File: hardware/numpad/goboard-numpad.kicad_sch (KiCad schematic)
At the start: 6 parts, among them J1 Conn_02x05_Top_Bottom, J2 Conn_01x01, J3 Conn_01x05, SW1 SW_Push

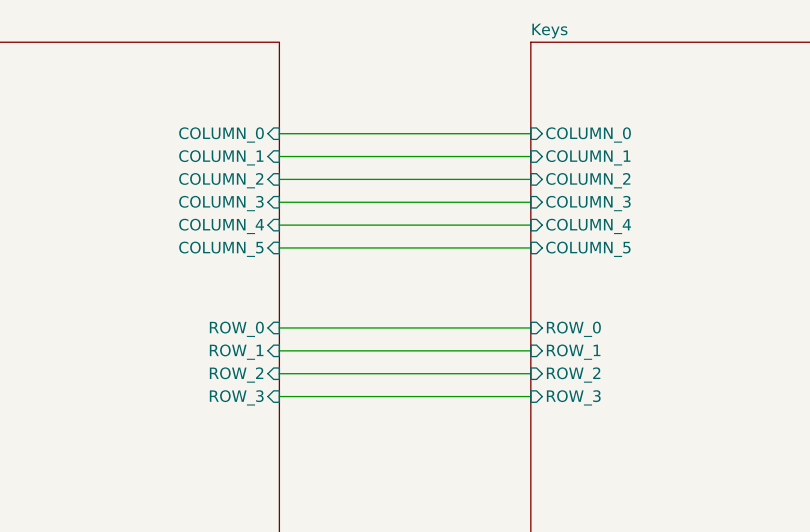
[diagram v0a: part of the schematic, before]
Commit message: Numpad: exchange key identifer
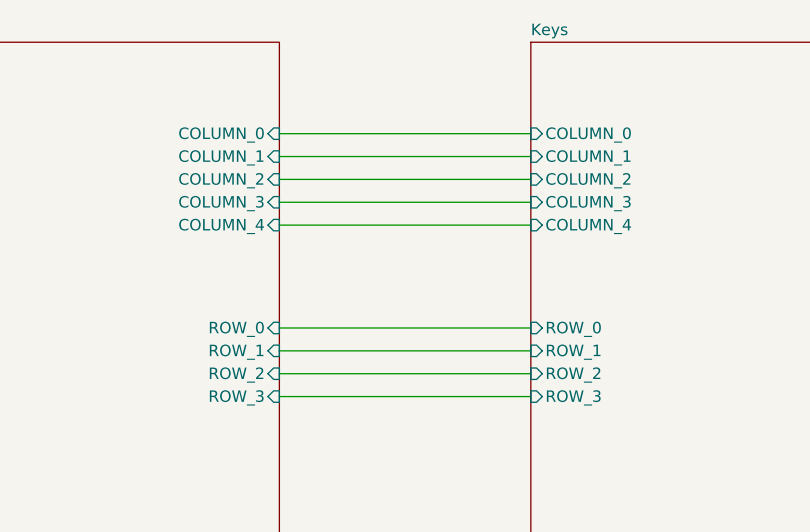
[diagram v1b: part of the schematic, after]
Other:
- sheet Keys ports: added none; removed COLUMN_5
- sheet mcu ports: added none; removed COLUMN_5
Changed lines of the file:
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@@
-    (stroke (width 0) (type solid) (color 0 0 0 0))
-  )
-  (wire (pts (xy 152.4 48.26) (xy 180.34 48.26))
     (stroke (width 0) (type solid) (color 0 0 0 0))
   )
@@
       (effects (font (size 1.27 1.27)) (justify left))
     )
-    (pin "COLUMN_5" input (at 180.34 48.26 180)
-      (effects (font (size 1.27 1.27)) (justify left))
-    )
     (pin "COLUMN_4" input (at 180.34 45.72 180)
       (effects (font (size 1.27 1.27)) (justify left))
@@
       (effects (font (size 1.27 1.27)) (justify left))
     )
-    (pin "COLUMN_5" input (at 152.4 48.26 0)
-      (effects (font (size 1.27 1.27)) (justify right))
-    )
     (pin "COLUMN_0" input (at 152.4 35.56 0)
       (effects (font (size 1.27 1.27)) (justify right))
@@
     )
     (path "/7cad715e-ebc0-41a5-9955-927ca63abd2f/6de5427d-4003-4de5-929c-849cf5d9ff9c"
-      (reference "SW8") (unit 1) (value "/") (footprint "footprints:SW_Cherry_MX_1.00u_PCB")
+      (reference "SW8") (unit 1) (value "divide") (footprint "footprints:SW_Cherry_MX_1.00u_PCB")
     )
     (path "/7cad715e-ebc0-41a5-9955-927ca63abd2f/72bf7a3c-a50c-4d69-90e7-2e5dba295699"
@@
     )
     (path "/7cad715e-ebc0-41a5-9955-927ca63abd2f/9b4a23f9-cd74-4ef8-8ec9-c324c0c6ccc0"
-      (reference "SW13") (unit 1) (value ".") (footprint "footprints:SW_Cherry_MX_1.00u_PCB")
+      (reference "SW13") (unit 1) (value "dot") (footprint "footprints:SW_Cherry_MX_1.00u_PCB")
     )
     (path "/7cad715e-ebc0-41a5-9955-927ca63abd2f/57a1dd78-2b07-42d9-8bd6-44368a92ec63"
-      (reference "SW14") (unit 1) (value "*") (footprint "footprints:SW_Cherry_MX_1.00u_PCB")
+      (reference "SW14") (unit 1) (value "times") (footprint "footprints:SW_Cherry_MX_1.00u_PCB")
     )
     (path "/7cad715e-ebc0-41a5-9955-927ca63abd2f/db6492b6-c0a9-4cb1-a618-b7fd084d31af"
@@
     )
     (path "/7cad715e-ebc0-41a5-9955-927ca63abd2f/4a471f23-a2bc-4fe0-b458-9d0b46d30813"
-      (reference "SW18") (unit 1) (value "-") (footprint "footprints:SW_Cherry_MX_1.00u_PCB")
+      (reference "SW18") (unit 1) (value "minus") (footprint "footprints:SW_Cherry_MX_1.00u_PCB")
     )
     (path "/7cad715e-ebc0-41a5-9955-927ca63abd2f/061c5f42-1869-4eb2-8fe0-4ae429f958da"
-      (reference "SW19") (unit 1) (value "+") (footprint "footprints:SW_Cherry_MX_2.00u_PCB")
+      (reference "SW19") (unit 1) (value "plus") (footprint "footprints:SW_Cherry_MX_2.00u_PCB")
     )
     (path "/7cad715e-ebc0-41a5-9955-927ca63abd2f/dcb7a6be-fb34-414c-ba21-e1f3767bdcea"

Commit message: Numpad: Fix labels of columns and rows of the key matrix
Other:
- sheet Keys ports: added ROW_4; removed COLUMN_4
- sheet mcu ports: added ROW_4; removed COLUMN_4
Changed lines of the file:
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@@
       (effects (font (size 1.27 1.27)) (justify left top))
     )
-    (pin "COLUMN_1" input (at 180.34 38.1 180)
+    (pin "COLUMN_1" input (at 180.34 59.69 180)
       (effects (font (size 1.27 1.27)) (justify left))
     )
-    (pin "COLUMN_0" input (at 180.34 35.56 180)
+    (pin "COLUMN_0" input (at 180.34 57.15 180)
       (effects (font (size 1.27 1.27)) (justify left))
     )
-    (pin "ROW_0" input (at 180.34 57.15 180)
+    (pin "ROW_0" input (at 180.34 35.56 180)
       (effects (font (size 1.27 1.27)) (justify left))
     )
-    (pin "ROW_1" input (at 180.34 59.69 180)
+    (pin "ROW_1" input (at 180.34 38.1 180)
       (effects (font (size 1.27 1.27)) (justify left))
     )
-    (pin "ROW_2" input (at 180.34 62.23 180)
+    (pin "ROW_2" input (at 180.34 40.64 180)
       (effects (font (size 1.27 1.27)) (justify left))
     )
-    (pin "ROW_3" input (at 180.34 64.77 180)
+    (pin "COLUMN_2" input (at 180.34 62.23 180)
       (effects (font (size 1.27 1.27)) (justify left))
     )
-    (pin "COLUMN_4" input (at 180.34 45.72 180)
+    (pin "COLUMN_3" input (at 180.34 64.77 180)
       (effects (font (size 1.27 1.27)) (justify left))
     )
-    (pin "COLUMN_2" input (at 180.34 40.64 180)
+    (pin "ROW_4" input (at 180.34 45.72 180)
       (effects (font (size 1.27 1.27)) (justify left))
     )
-    (pin "COLUMN_3" input (at 180.34 43.18 180)
+    (pin "ROW_3" input (at 180.34 43.18 180)
       (effects (font (size 1.27 1.27)) (justify left))
     )
@@
       (effects (font (size 1.27 1.27)) (justify left top))
     )
-    (pin "ROW_1" input (at 152.4 59.69 0)
+    (pin "ROW_1" input (at 152.4 38.1 0)
       (effects (font (size 1.27 1.27)) (justify right))
     )
-    (pin "ROW_2" input (at 152.4 62.23 0)
+    (pin "ROW_2" input (at 152.4 40.64 0)
       (effects (font (size 1.27 1.27)) (justify right))
     )
-    (pin "ROW_0" input (at 152.4 57.15 0)
+    (pin "ROW_0" input (at 152.4 35.56 0)
       (effects (font (size 1.27 1.27)) (justify right))
     )
-    (pin "ROW_3" input (at 152.4 64.77 0)
+    (pin "ROW_3" input (at 152.4 43.18 0)
       (effects (font (size 1.27 1.27)) (justify right))
     )
@@
       (effects (font (size 1.27 1.27)) (justify left))
     )
-    (pin "COLUMN_0" input (at 152.4 35.56 0)
+    (pin "COLUMN_0" input (at 152.4 57.15 0)
       (effects (font (size 1.27 1.27)) (justify right))
     )
-    (pin "COLUMN_4" input (at 152.4 45.72 0)
+    (pin "COLUMN_1" input (at 152.4 59.69 0)
       (effects (font (size 1.27 1.27)) (justify right))
     )
-    (pin "COLUMN_1" input (at 152.4 38.1 0)
+    (pin "COLUMN_3" input (at 152.4 64.77 0)
       (effects (font (size 1.27 1.27)) (justify right))
     )
-    (pin "COLUMN_3" input (at 152.4 43.18 0)
-      (effects (font (size 1.27 1.27)) (justify right))
-    )
-    (pin "COLUMN_2" input (at 152.4 40.64 0)
+    (pin "COLUMN_2" input (at 152.4 62.23 0)
       (effects (font (size 1.27 1.27)) (justify right))
     )
@@
       (effects (font (size 1.27 1.27)) (justify left))
     )
+    (pin "ROW_4" input (at 152.4 45.72 0)
+      (effects (font (size 1.27 1.27)) (justify right))
+    )
   )

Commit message: Numpad: Exchange the debug-conn footprint for one without silkscreen
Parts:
- J1: footprint footprints:programming_port_st_link_clone -> footprints:programming_port_st_link_clone_without_silkscreen_outline
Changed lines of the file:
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@@
     (property "Reference" "J1" (id 0) (at 52.07 111.76 0))
     (property "Value" "Conn_02x05_Top_Bottom" (id 1) (at 52.07 109.22 0))
-    (property "Footprint" "footprints:programming_port_st_link_clone" (id 2) (at 50.8 100.33 0)
+    (property "Footprint" "footprints:programming_port_st_link_clone_without_silkscreen_outline" (id 2) (at 50.8 100.33 0)
       (effects (font (size 1.27 1.27)) hide)
     )
@@
     )
     (path "/15258cf0-82ec-42ff-b81f-96479422bf94"
-      (reference "J1") (unit 1) (value "Conn_02x05_Top_Bottom") (footprint "footprints:programming_port_st_link_clone")
+      (reference "J1") (unit 1) (value "Conn_02x05_Top_Bottom") (footprint "footprints:programming_port_st_link_clone_without_silkscreen_outline")
     )
     (path "/f8d99eaa-eaec-4e45-8350-19b611a4fda8"

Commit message: Numpad: Add missing part numbers
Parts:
- C1: Mouser (none) -> 581-0603YC104MAT4A; Part Name (none) -> AVX 0603YC104MAT4A
- J1, J2, J3: Mouser (none) -> -; Part Name (none) -> -
- SW1: Mouser (none) -> 611-PTS636SM25SMTRLF; Part Name (none) -> PTS636 SM25 SMTR LFS
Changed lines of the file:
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@@
+      (effects (font (size 1.27 1.27)) hide)
+    )
+    (property "Mouser" "-" (id 4) (at 50.8 119.38 0)
+      (effects (font (size 1.27 1.27)) hide)
+    )
+    (property "Part Name" "-" (id 5) (at 50.8 119.38 0)
       (effects (font (size 1.27 1.27)) hide)
     )
@@
     )
     (property "Datasheet" "~" (id 3) (at 38.1 144.78 0)
+      (effects (font (size 1.27 1.27)) hide)
+    )
+    (property "Mouser" "581-0603YC104MAT4A" (id 4) (at 38.1 144.78 0)
+      (effects (font (size 1.27 1.27)) hide)
+    )
+    (property "Part Name" "AVX 0603YC104MAT4A" (id 5) (at 38.1 144.78 0)
       (effects (font (size 1.27 1.27)) hide)
     )
@@
       (effects (font (size 1.27 1.27)) hide)
     )
-    (property "Datasheet" "~" (id 3) (at 45.72 135.89 0)
+    (property "Datasheet" "https://www.mouser.de/datasheet/2/60/pts636-1550567.pdf" (id 3) (at 45.72 135.89 0)
+      (effects (font (size 1.27 1.27)) hide)
+    )
+    (property "Mouser" "611-PTS636SM25SMTRLF" (id 4) (at 45.72 140.97 0)
+      (effects (font (size 1.27 1.27)) hide)
+    )
+    (property "Part Name" "PTS636 SM25 SMTR LFS" (id 5) (at 45.72 140.97 0)
       (effects (font (size 1.27 1.27)) hide)
     )
@@
       (effects (font (size 1.27 1.27)) hide)
     )
+    (property "Mouser" "-" (id 4) (at 24.13 39.37 0)
+      (effects (font (size 1.27 1.27)) hide)
+    )
+    (property "Part Name" "-" (id 5) (at 24.13 39.37 0)
+      (effects (font (size 1.27 1.27)) hide)
+    )
     (pin "1")
     (pin "2")
@@
     )
     (property "Datasheet" "~" (id 3) (at 50.8 100.33 0)
+      (effects (font (size 1.27 1.27)) hide)
+    )
+    (property "Mouser" "-" (id 4) (at 50.8 100.33 0)
+      (effects (font (size 1.27 1.27)) hide)
+    )
+    (property "Part Name" "-" (id 5) (at 50.8 100.33 0)
       (effects (font (size 1.27 1.27)) hide)
     )
@@
     )
     (path "/abe4c75b-07ed-49c0-b60b-44793e4dbe28/1aa302d2-19e0-43fb-b295-50799f1dd6de"
-      (reference "C3") (unit 1) (value "10u") (footprint "Capacitor_SMD:C_0603_1608Metric_Pad1.08x0.95mm_HandSolder")
+      (reference "C3") (unit 1) (value "10u") (footprint "Capacitor_SMD:C_0805_2012Metric")
     )
     (path "/abe4c75b-07ed-49c0-b60b-44793e4dbe28/9fd0a2f4-36bb-4982-8a0e-e6abf88ca2c7"
@@
     )
     (path "/abe4c75b-07ed-49c0-b60b-44793e4dbe28/a428fde3-799b-45e1-885c-a2e74db1f5cd"
-      (reference "C5") (unit 1) (value "10u") (footprint "Capacitor_SMD:C_0603_1608Metric_Pad1.08x0.95mm_HandSolder")
+      (reference "C5") (unit 1) (value "10u") (footprint "Capacitor_SMD:C_0805_2012Metric")
     )
     (path "/abe4c75b-07ed-49c0-b60b-44793e4dbe28/57b040a2-5a62-4a91-a02e-69a209e228e4"

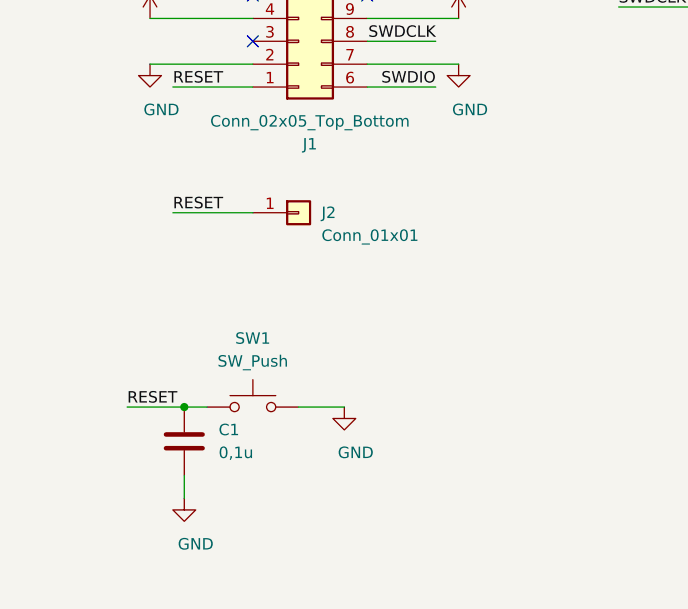
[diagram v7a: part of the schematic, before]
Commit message: Numpad: Add pullup for reset and connect BOOT0 to ground
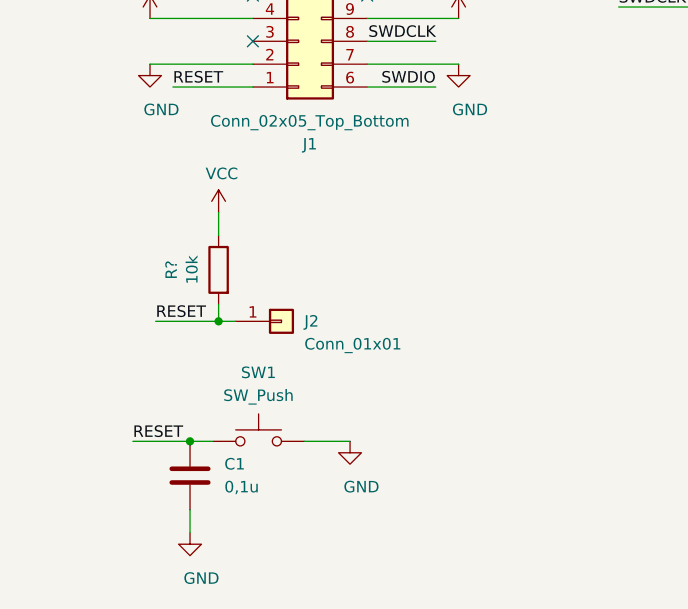
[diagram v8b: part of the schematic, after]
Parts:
- added R?: 10k, Resistor_SMD:R_0603_1608Metric_Pad0.98x0.95mm_HandSolder, symbol Device:R
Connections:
- net RESET: now also R?.2
- net VCC: now also R?.1
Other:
- moved on the sheet: C1, J2, SW1
